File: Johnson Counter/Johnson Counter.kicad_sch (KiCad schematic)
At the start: 4 parts, among them J101 USB_A

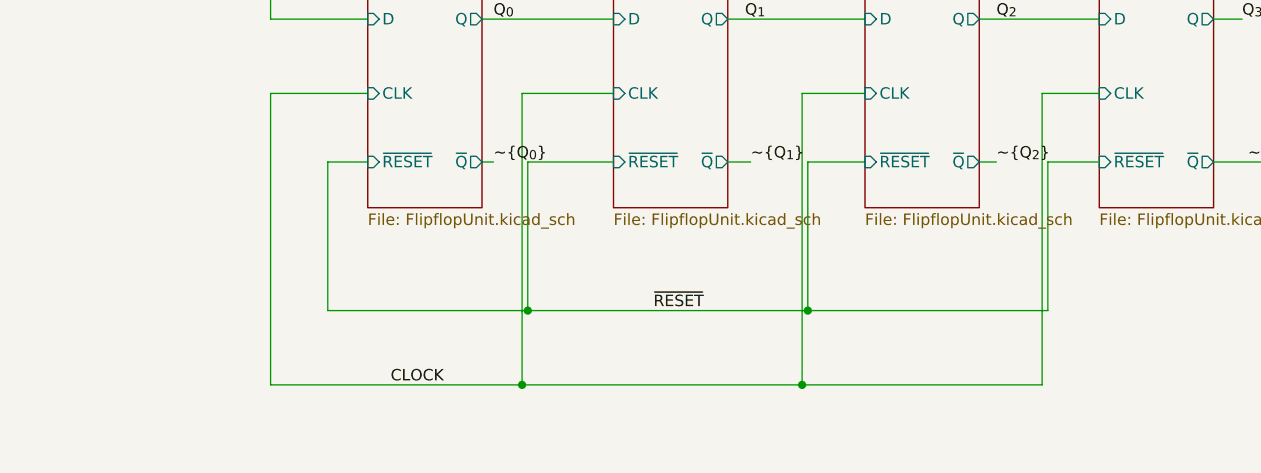
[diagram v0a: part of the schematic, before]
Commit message: Adding the clock push button
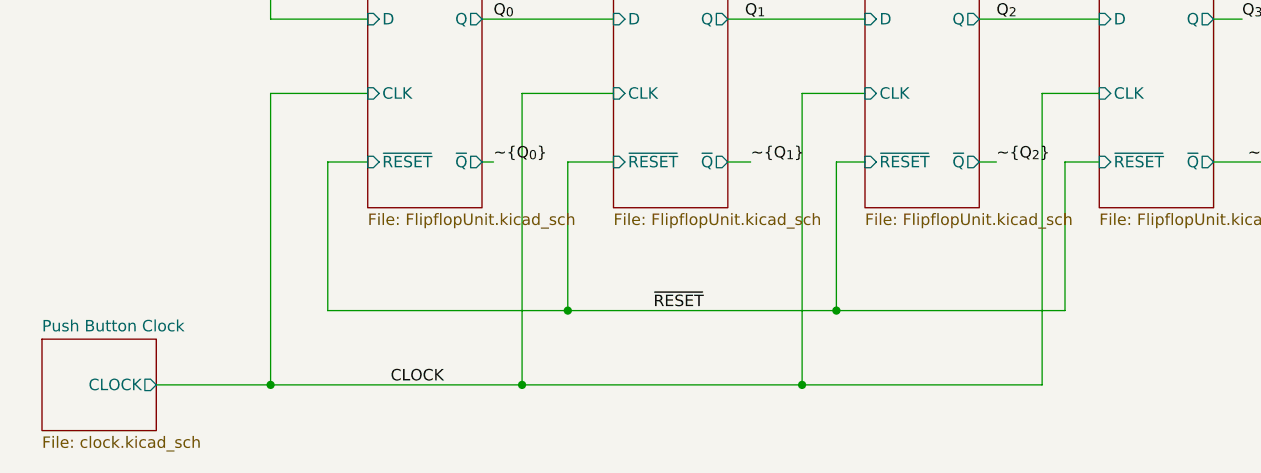
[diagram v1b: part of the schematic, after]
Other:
- added sheet Push Button Clock (clock.kicad_sch)
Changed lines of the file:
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@@
   (junction (at 217.17 135.255) (diameter 0) (color 0 0 0 0)
   )
-  (junction (at 85.725 162.56) (diameter 0) (color 0 0 0 0)
+  (junction (at 90.17 162.56) (diameter 0) (color 0 0 0 0)
+  )
+  (junction (at 120.015 162.56) (diameter 0) (color 0 0 0 0)
   )
   (junction (at 217.17 147.955) (diameter 0) (color 0 0 0 0)
   )
-  (junction (at 116.84 162.56) (diameter 0) (color 0 0 0 0)
+  (junction (at 57.15 170.815) (diameter 0) (color 0 0 0 0)
   )
   (junction (at 49.53 28.575) (diameter 0) (color 0 0 0 0)
@@
     (stroke (width 0) (type default) (color 0 0 0 0))
   )
+  (wire (pts (xy 120.015 162.56) (xy 145.415 162.56))
+    (stroke (width 0) (type default) (color 0 0 0 0))
+  )
+  (wire (pts (xy 145.415 146.05) (xy 149.225 146.05))
+    (stroke (width 0) (type default) (color 0 0 0 0))
+  )
   (wire (pts (xy 67.945 138.43) (xy 57.15 138.43))
     (stroke (width 0) (type default) (color 0 0 0 0))
@@
     (stroke (width 0) (type default) (color 0 0 0 0))
   )
+  (wire (pts (xy 123.19 146.05) (xy 120.015 146.05))
+    (stroke (width 0) (type default) (color 0 0 0 0))
+  )
+  (wire (pts (xy 44.45 170.815) (xy 57.15 170.815))
+    (stroke (width 0) (type default) (color 0 0 0 0))
+  )
   (wire (pts (xy 34.29 45.085) (xy 34.29 47.625))
     (stroke (width 0) (type default) (color 0 0 0 0))
@@
     (stroke (width 0) (type default) (color 0 0 0 0))
   )
+  (wire (pts (xy 120.015 146.05) (xy 120.015 162.56))
+    (stroke (width 0) (type default) (color 0 0 0 0))
+  )
   (wire (pts (xy 217.17 147.955) (xy 229.87 147.955))
     (stroke (width 0) (type default) (color 0 0 0 0))
@@
     (stroke (width 0) (type default) (color 0 0 0 0))
   )
-  (wire (pts (xy 95.25 146.05) (xy 85.725 146.05))
-    (stroke (width 0) (type default) (color 0 0 0 0))
-  )
-  (wire (pts (xy 85.725 162.56) (xy 116.84 162.56))
-    (stroke (width 0) (type default) (color 0 0 0 0))
-  )
   (wire (pts (xy 34.29 43.815) (xy 34.29 45.085))
     (stroke (width 0) (type default) (color 0 0 0 0))
@@
     (stroke (width 0) (type default) (color 0 0 0 0))
   )
-  (wire (pts (xy 143.51 162.56) (xy 143.51 146.05))
-    (stroke (width 0) (type default) (color 0 0 0 0))
-  )
-  (wire (pts (xy 63.5 162.56) (xy 85.725 162.56))
+  (wire (pts (xy 63.5 162.56) (xy 90.17 162.56))
     (stroke (width 0) (type default) (color 0 0 0 0))
   )
@@
     (stroke (width 0) (type default) (color 0 0 0 0))
   )
+  (wire (pts (xy 145.415 162.56) (xy 145.415 146.05))
+    (stroke (width 0) (type default) (color 0 0 0 0))
+  )
   (wire (pts (xy 63.5 146.05) (xy 63.5 162.56))
     (stroke (width 0) (type default) (color 0 0 0 0))
@@
     (stroke (width 0) (type default) (color 0 0 0 0))
   )
-  (wire (pts (xy 116.84 146.05) (xy 123.19 146.05))
-    (stroke (width 0) (type default) (color 0 0 0 0))
-  )
   (wire (pts (xy 41.91 36.195) (xy 46.99 36.195))
     (stroke (width 0) (type default) (color 0 0 0 0))
@@
     (stroke (width 0) (type default) (color 0 0 0 0))
   )
-  (wire (pts (xy 143.51 146.05) (xy 149.225 146.05))
+  (wire (pts (xy 90.17 162.56) (xy 120.015 162.56))
     (stroke (width 0) (type default) (color 0 0 0 0))
   )
@@
     (stroke (width 0) (type default) (color 0 0 0 0))
   )
-  (wire (pts (xy 116.84 162.56) (xy 116.84 146.05))
-    (stroke (width 0) (type default) (color 0 0 0 0))
-  )
   (wire (pts (xy 161.925 130.175) (xy 165.1 130.175))
     (stroke (width 0) (type default) (color 0 0 0 0))
   )
-  (wire (pts (xy 85.725 146.05) (xy 85.725 162.56))
+  (wire (pts (xy 90.17 146.05) (xy 90.17 162.56))
     (stroke (width 0) (type default) (color 0 0 0 0))
   )
@@
     (stroke (width 0) (type default) (color 0 0 0 0))
   )
-  (wire (pts (xy 116.84 162.56) (xy 143.51 162.56))
+  (wire (pts (xy 95.25 146.05) (xy 90.17 146.05))
     (stroke (width 0) (type default) (color 0 0 0 0))
   )
@@
     )
     (pin "Q" output (at 80.645 130.175 0)
+      (effects (font (size 1.27 1.27)) (justify right))
+    )
+  )
+  (sheet (at 31.75 165.735) (size 12.7 10.16) (fields_autoplaced)
+    (stroke (width 0.1524) (type solid) (color 0 0 0 0))
+    (fill (color 0 0 0 0.0000))
+    (property "Sheet name" "Push Button Clock" (id 0) (at 31.75 165.0234 0)
+      (effects (font (size 1.27 1.27)) (justify left bottom))
+    )
+    (property "Sheet file" "clock.kicad_sch" (id 1) (at 31.75 176.4796 0)
+      (effects (font (size 1.27 1.27)) (justify left top))
+    )
+    (pin "CLOCK" output (at 44.45 170.815 0)
       (effects (font (size 1.27 1.27)) (justify right))
     )
@@
     (path "/1776560d-d10e-49df-958c-2ec91c20f090" (page "4"))
     (path "/61a6eaa9-6d31-4a13-9431-a85264c68c90" (page "5"))
+    (path "/be64a935-e1ad-4178-8df9-3a3a692146ca" (page "6"))
   )
   (symbol_instances
@@
       (reference "#PWR0128") (unit 1) (value "GND") (footprint "")
     )
+    (path "/be64a935-e1ad-4178-8df9-3a3a692146ca/f1d0e682-c3b0-48ff-800c-ae4c05fb7c59"
+      (reference "#PWR?") (unit 1) (value "+5V") (footprint "")
+    )
     (path "/6805fa98-1af3-400d-8ee1-942ec0bda00d"
       (reference "C101") (unit 1) (value "10u") (footprint "Capacitor_THT:CP_Radial_D4.0mm_P1.50mm")
@@
       (reference "C501") (unit 1) (value "100n") (footprint "Capacitor_THT:C_Disc_D5.0mm_W2.5mm_P5.00mm")
     )
+    (path "/be64a935-e1ad-4178-8df9-3a3a692146ca/41a57fed-b183-47c9-9866-3cea0d6f64a1"
+      (reference "C?") (unit 1) (value "10nF") (footprint "Capacitor_THT:C_Disc_D3.0mm_W2.0mm_P2.50mm")
+    )
+    (path "/be64a935-e1ad-4178-8df9-3a3a692146ca/f9630321-33ef-4723-8a9f-39985125b716"
+      (reference "C?") (unit 1) (value "0.1u") (footprint "Capacitor_THT:C_Disc_D4.7mm_W2.5mm_P5.00mm")
+    )
     (path "/9dc7180d-0fb6-462e-a6b3-ff1204ad5b42/fa856644-8a5c-4b6a-af5b-26a730f71c3f"
       (reference "D201") (unit 1) (value "LED") (footprint "LED_THT:LED_D3.0mm")
@@
       (reference "R502") (unit 1) (value "4k7") (footprint "Resistor_THT:R_Axial_DIN0207_L6.3mm_D2.5mm_P7.62mm_Horizontal")
     )
+    (path "/be64a935-e1ad-4178-8df9-3a3a692146ca/055a220e-fa95-4eac-85b8-aeeb1345565a"
+      (reference "R?") (unit 1) (value "22k") (footprint "Resistor_THT:R_Axial_DIN0207_L6.3mm_D2.5mm_P7.62mm_Horizontal")
+    )
+    (path "/be64a935-e1ad-4178-8df9-3a3a692146ca/cf5d25ee-c8ff-4b44-8550-332a25717421"
+      (reference "R?") (unit 1) (value "1M") (footprint "Resistor_THT:R_Axial_DIN0207_L6.3mm_D2.5mm_P7.62mm_Horizontal")
+    )
     (path "/9dc7180d-0fb6-462e-a6b3-ff1204ad5b42/f693bfaf-70f9-4542-8d41-0ba87a0a8d8c"
       (reference "U201") (unit 1) (value "74HC74") (footprint "Package_DIP:DIP-14_W7.62mm_Socket")
@@
       (reference "U501") (unit 3) (value "74HC74") (footprint "")
     )
-  )
+    (path "/be64a935-e1ad-4178-8df9-3a3a692146ca/63be3227-0a9b-462a-8791-8e16c30ba050"
+      (reference "U?") (unit 1) (value "+5V") (footprint "")
+    )
+    (path "/be64a935-e1ad-4178-8df9-3a3a692146ca/a509a93b-89f8-406d-8c6e-4cb9c4fd27ff"
+      (reference "U?") (unit 1) (value "GND") (footprint "")
+    )
+    (path "/be64a935-e1ad-4178-8df9-3a3a692146ca/c489bb15-165b-43a6-94b6-49adb8c893ed"
+      (reference "U?") (unit 1) (value "SW_Push") (footprint "Button_Switch_THT:SW_PUSH_6mm_H4.3mm")
+    )
+    (path "/be64a935-e1ad-4178-8df9-3a3a692146ca/d8b2a887-34fb-4bf2-8587-aaf9dae97ab2"
+      (reference "U?") (unit 1) (value "LM555xM") (footprint "Package_DIP:DIP-8_W7.62mm_Socket")
+    )
+  )

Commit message: Working on decoder stage
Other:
- added sheet Decoder (decoder.kicad_sch)

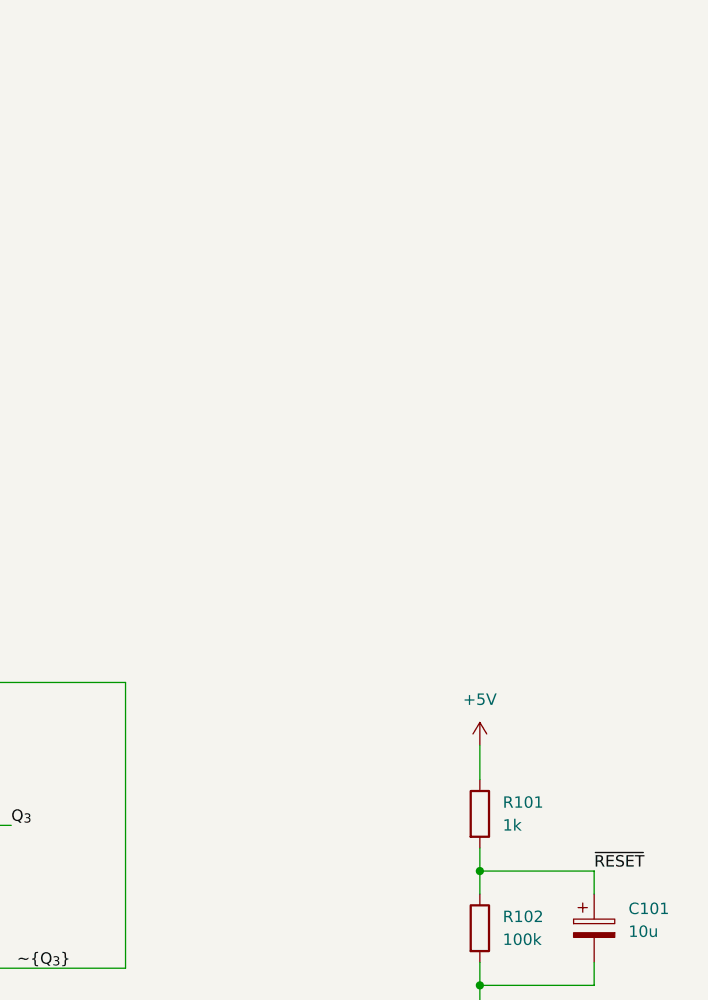
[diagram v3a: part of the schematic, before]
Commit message: Finishing routing, silkscreen and mounting
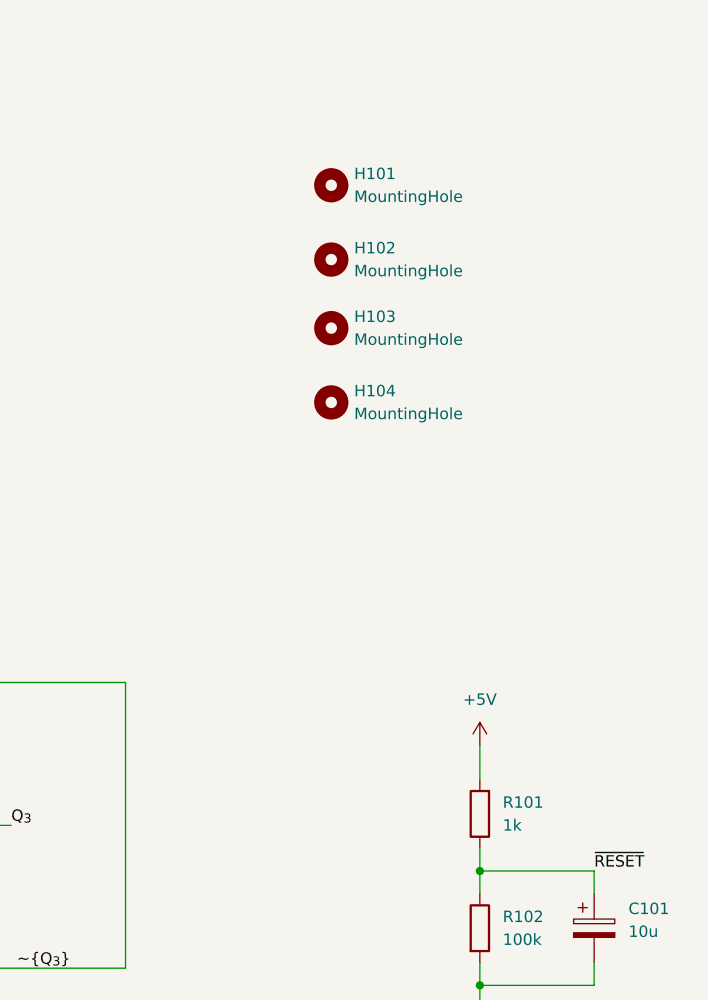
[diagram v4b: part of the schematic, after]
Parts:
- added H101, H102, H103, H104: MountingHole, MountingHole:MountingHole_2.2mm_M2, symbol Mechanical:MountingHole
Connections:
- net +5V: now also R101.2; no longer R101.1
- net ~{RESET}: now also R101.1; no longer R101.2
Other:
- moved on the sheet: R101
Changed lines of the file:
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@@
     (effects (font (size 1.27 1.27)) (justify right bottom))
+  )
+  (symbol (lib_id "Mechanical:MountingHole") (at 200.66 83.185 0) (unit 1)
+    (in_bom yes) (on_board yes) (fields_autoplaced)
+    (property "Reference" "H104" (id 0) (at 203.2 81.9149 0)
+      (effects (font (size 1.27 1.27)) (justify left))
+    )
+    (property "Value" "MountingHole" (id 1) (at 203.2 84.4549 0)
+      (effects (font (size 1.27 1.27)) (justify left))
+    )
+    (property "Footprint" "MountingHole:MountingHole_2.2mm_M2" (id 2) (at 200.66 83.185 0)
+      (effects (font (size 1.27 1.27)) hide)
+    )
+    (property "Datasheet" "~" (id 3) (at 200.66 83.185 0)
+      (effects (font (size 1.27 1.27)) hide)
+    )
   )
   (symbol (lib_id "power:GND") (at 217.17 150.495 0) (unit 1)
@@
     (pin "1")
     (pin "2")
+  )
+  (symbol (lib_id "Mechanical:MountingHole") (at 200.66 67.31 0) (unit 1)
+    (in_bom yes) (on_board yes) (fields_autoplaced)
+    (property "Reference" "H102" (id 0) (at 203.2 66.0399 0)
+      (effects (font (size 1.27 1.27)) (justify left))
+    )
+    (property "Value" "MountingHole" (id 1) (at 203.2 68.5799 0)
+      (effects (font (size 1.27 1.27)) (justify left))
+    )
+    (property "Footprint" "MountingHole:MountingHole_2.2mm_M2" (id 2) (at 200.66 67.31 0)
+      (effects (font (size 1.27 1.27)) hide)
+    )
+    (property "Datasheet" "~" (id 3) (at 200.66 67.31 0)
+      (effects (font (size 1.27 1.27)) hide)
+    )
   )
   (symbol (lib_id "power:PWR_FLAG") (at 49.53 28.575 0) (unit 1)
@@
     (pin "1")
   )
+  (symbol (lib_id "Mechanical:MountingHole") (at 200.66 74.93 0) (unit 1)
+    (in_bom yes) (on_board yes) (fields_autoplaced)
+    (property "Reference" "H103" (id 0) (at 203.2 73.6599 0)
+      (effects (font (size 1.27 1.27)) (justify left))
+    )
+    (property "Value" "MountingHole" (id 1) (at 203.2 76.1999 0)
+      (effects (font (size 1.27 1.27)) (justify left))
+    )
+    (property "Footprint" "MountingHole:MountingHole_2.2mm_M2" (id 2) (at 200.66 74.93 0)
+      (effects (font (size 1.27 1.27)) hide)
+    )
+    (property "Datasheet" "~" (id 3) (at 200.66 74.93 0)
+      (effects (font (size 1.27 1.27)) hide)
+    )
+  )
+  (symbol (lib_id "Mechanical:MountingHole") (at 200.66 59.055 0) (unit 1)
+    (in_bom yes) (on_board yes) (fields_autoplaced)
+    (property "Reference" "H101" (id 0) (at 203.2 57.7849 0)
+      (effects (font (size 1.27 1.27)) (justify left))
+    )
+    (property "Value" "MountingHole" (id 1) (at 203.2 60.3249 0)
+      (effects (font (size 1.27 1.27)) (justify left))
+    )
+    (property "Footprint" "MountingHole:MountingHole_2.2mm_M2" (id 2) (at 200.66 59.055 0)
+      (effects (font (size 1.27 1.27)) hide)
+    )
+    (property "Datasheet" "~" (id 3) (at 200.66 59.055 0)
+      (effects (font (size 1.27 1.27)) hide)
+    )
+  )
   (symbol (lib_id "power:+5V") (at 62.23 24.765 0) (unit 1)
     (in_bom yes) (on_board yes) (fields_autoplaced)
@@
     (pin "1")
   )
-  (symbol (lib_id "Device:R") (at 217.17 128.905 0) (unit 1)
+  (symbol (lib_id "Device:R") (at 217.17 128.905 180) (unit 1)
     (in_bom yes) (on_board yes) (fields_autoplaced)
     (property "Reference" "R101" (id 0) (at 219.71 127.6349 0)
-      (effects (font (size 1.27 1.27)) (justify left))
+      (effects (font (size 1.27 1.27)) (justify right))
     )
     (property "Value" "1k" (id 1) (at 219.71 130.1749 0)
-      (effects (font (size 1.27 1.27)) (justify left))
-    )
-    (property "Footprint" "Resistor_THT:R_Axial_DIN0207_L6.3mm_D2.5mm_P7.62mm_Horizontal" (id 2) (at 215.392 128.905 90)
+      (effects (font (size 1.27 1.27)) (justify right))
+    )
+    (property "Footprint" "Resistor_THT:R_Axial_DIN0207_L6.3mm_D2.5mm_P7.62mm_Horizontal" (id 2) (at 218.948 128.905 90)
       (effects (font (size 1.27 1.27)) hide)
     )
@@
       (reference "D708") (unit 1) (value "LED") (footprint "LED_THT:LED_D5.0mm")
     )
+    (path "/d49e712d-4f89-4605-ae38-3303b8d0d523"
+      (reference "H101") (unit 1) (value "MountingHole") (footprint "MountingHole:MountingHole_2.2mm_M2")
+    )
+    (path "/748f8ed8-3603-4869-ac94-819b82781ea9"
+      (reference "H102") (unit 1) (value "MountingHole") (footprint "MountingHole:MountingHole_2.2mm_M2")
+    )
+    (path "/c7b045ab-4765-4443-a035-f9469e49647e"
+      (reference "H103") (unit 1) (value "MountingHole") (footprint "MountingHole:MountingHole_2.2mm_M2")
+    )
+    (path "/14507af9-69cb-4a28-841d-0aac9cb3b1be"
+      (reference "H104") (unit 1) (value "MountingHole") (footprint "MountingHole:MountingHole_2.2mm_M2")
+    )
     (path "/b5fe11d7-adca-4f5f-ba37-a45cf58372d9"
